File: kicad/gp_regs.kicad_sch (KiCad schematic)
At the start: 12 parts, among them SW2 SW_SPST, SW3 SW_SPST, SW4 SW_SPST, SW5 SW_SPST

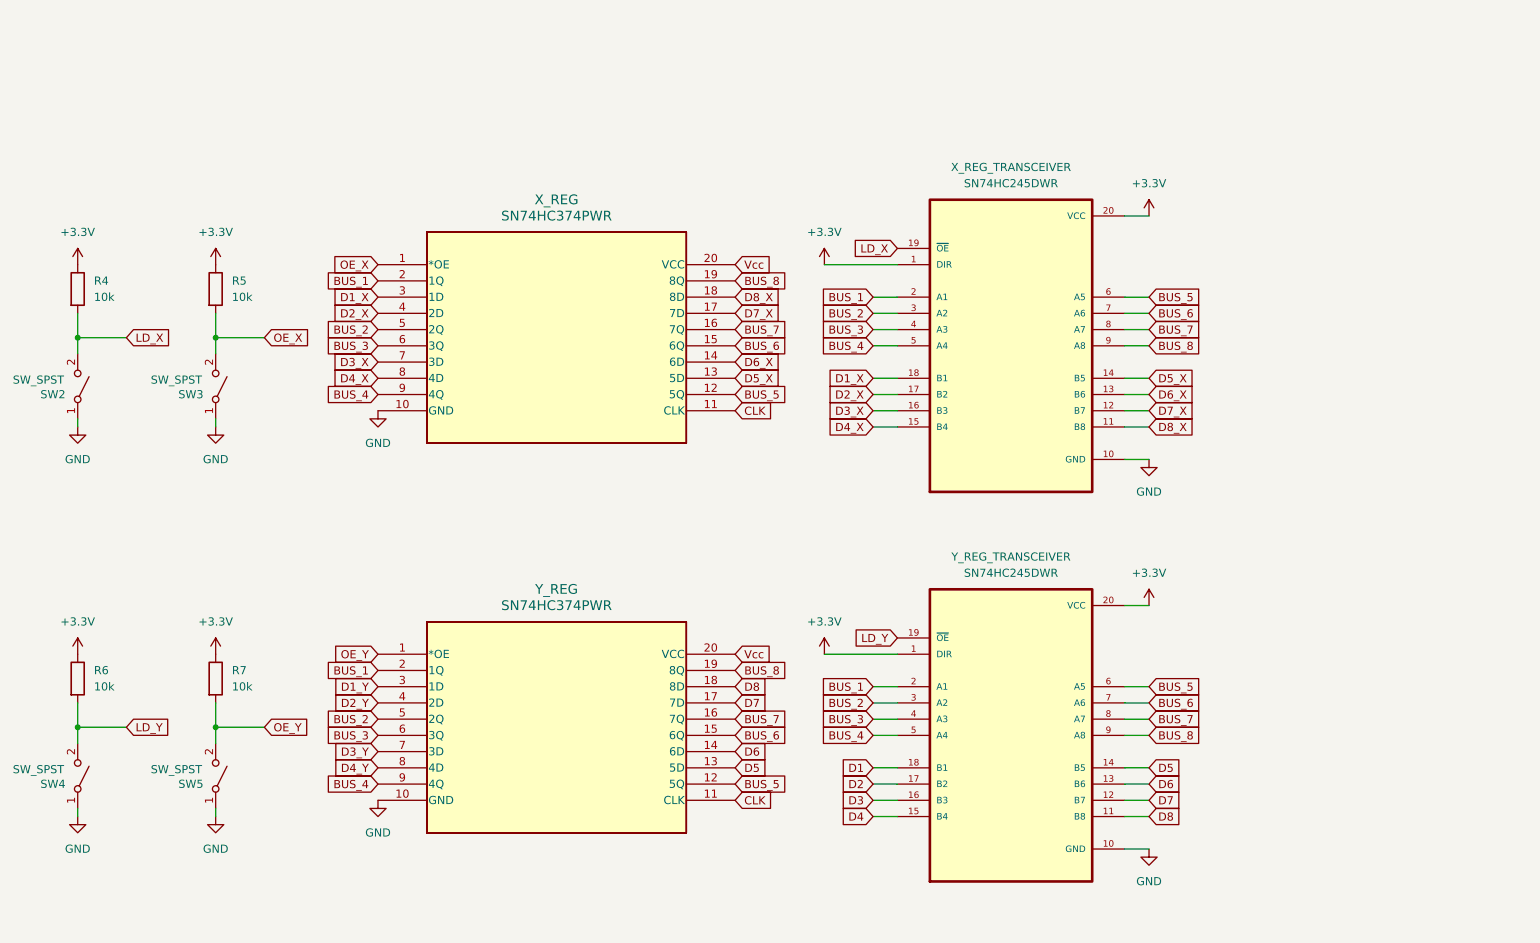
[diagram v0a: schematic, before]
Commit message: update schematic
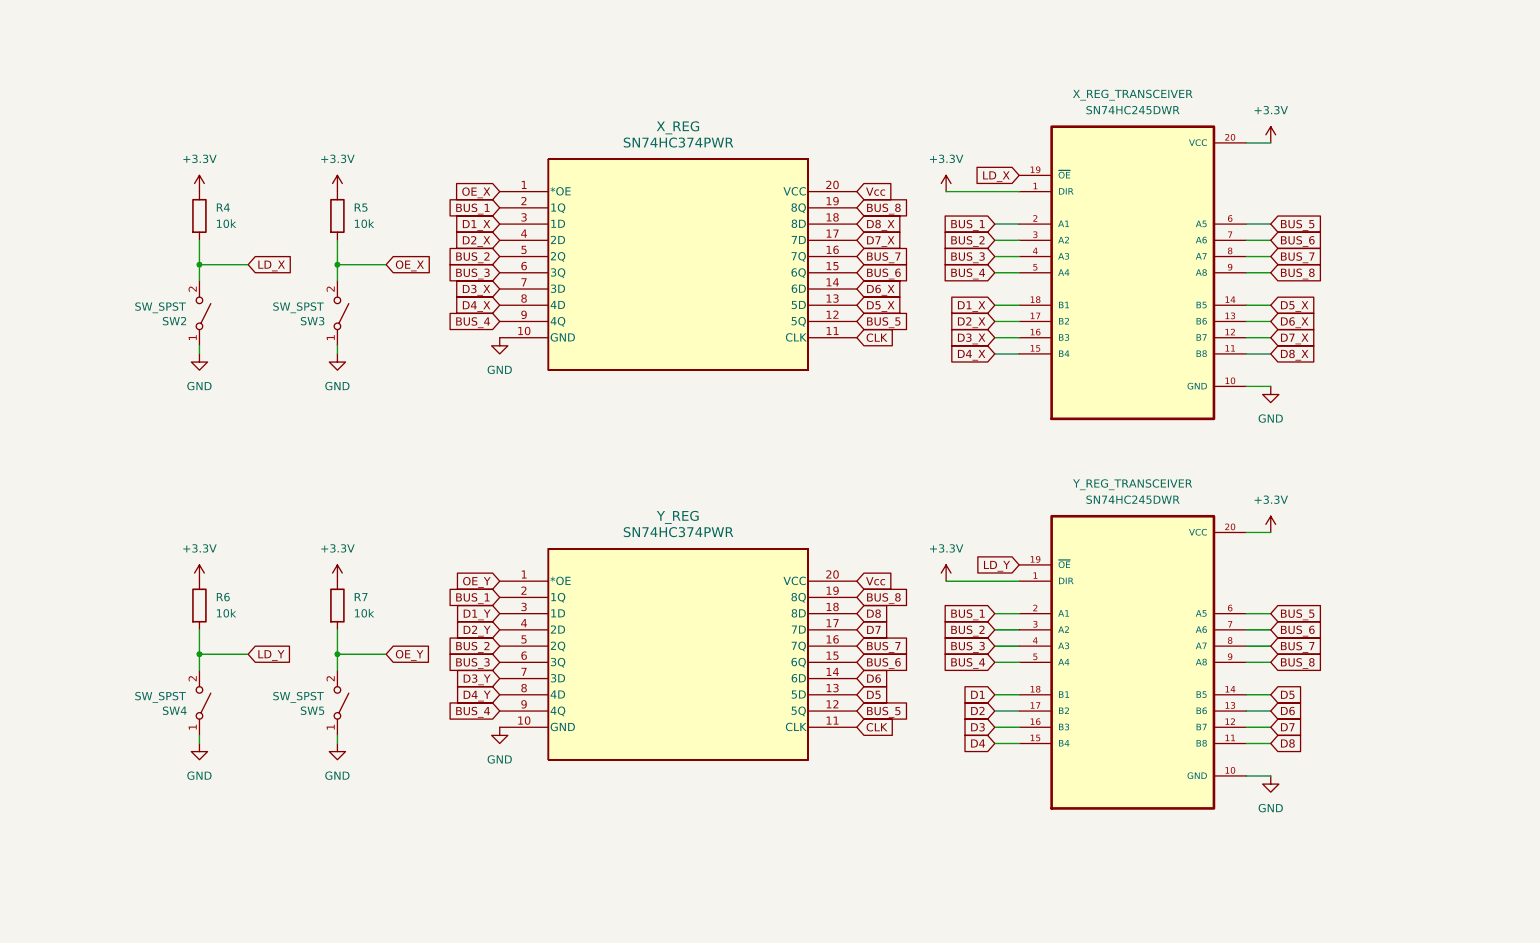
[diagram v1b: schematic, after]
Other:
- moved on the sheet: R4, R5, R6, R7, SW2, SW3, SW4, SW5, X_REG, X_REG_TRANSCEIVER, Y_REG, Y_REG_TRANSCEIVER

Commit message: update schematic
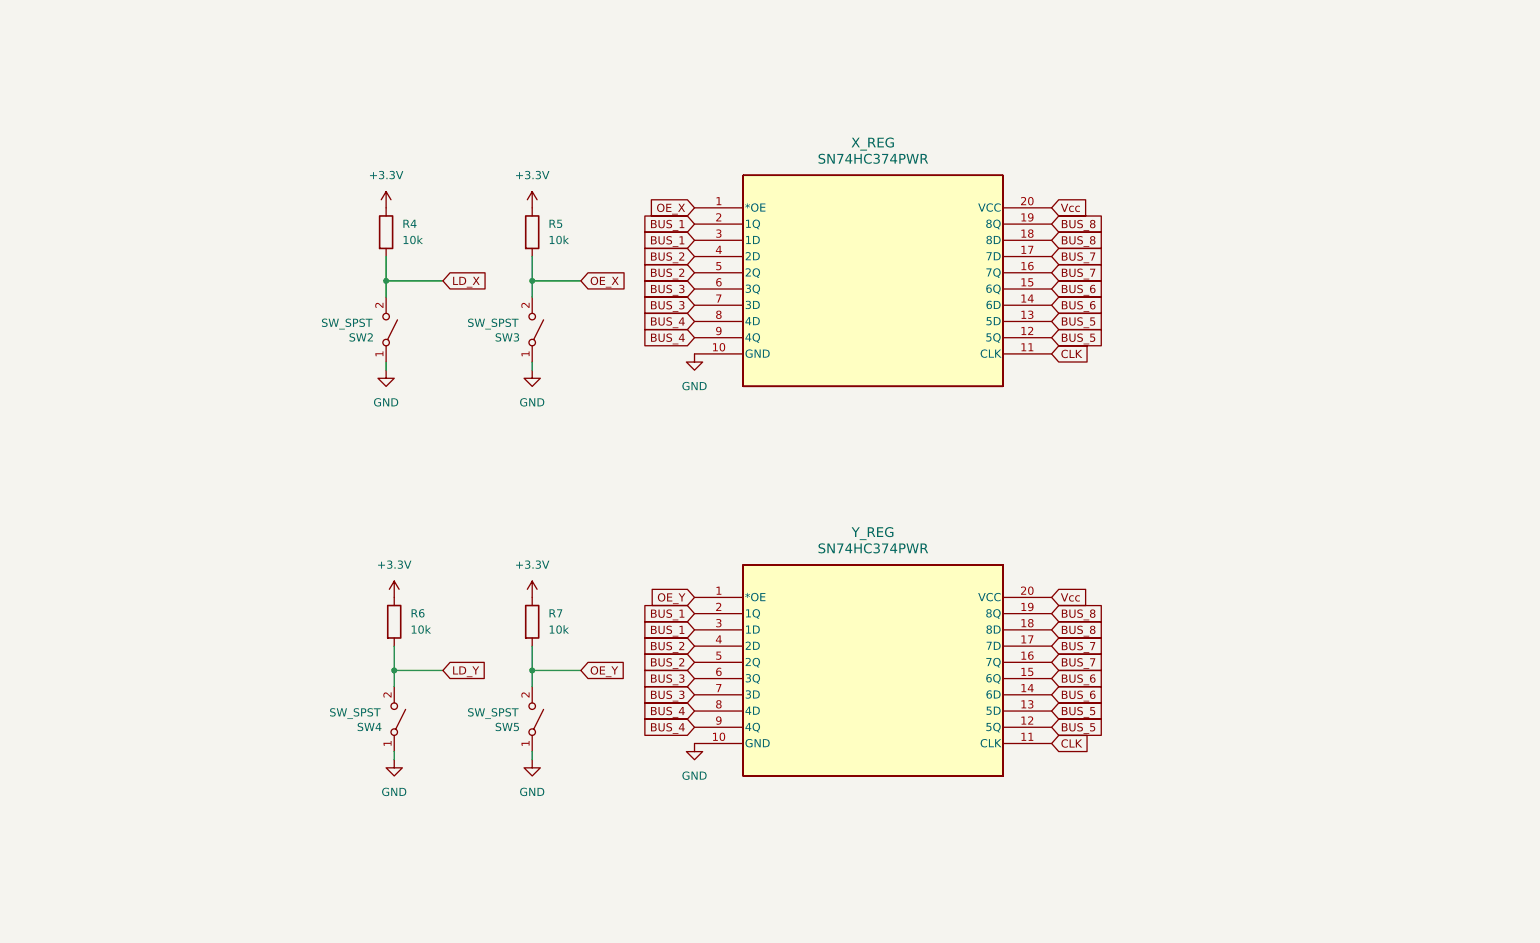
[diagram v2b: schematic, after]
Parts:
- removed X_REG_TRANSCEIVER, Y_REG_TRANSCEIVER: SN74HC245DWR, SN74HC245DWR:SOIC127P1030X265-20N, symbol SN74HC245DWR:SN74HC245DWR
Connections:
- net D1_X is gone; now on net BUS_1: X_REG.3 (1D)
- net D1_Y is gone; now on net BUS_1: Y_REG.3 (1D)
- net D2_X is gone; now on net BUS_2: X_REG.4 (2D)
- net D2_Y is gone; now on net BUS_2: Y_REG.4 (2D)
- net D3_X is gone; now on net BUS_3: X_REG.7 (3D)
- net D3_Y is gone; now on net BUS_3: Y_REG.7 (3D)
- net D4_X is gone; now on net BUS_4: X_REG.8 (4D)
- net D4_Y is gone; now on net BUS_4: Y_REG.8 (4D)
- net D5 is gone; now on net BUS_5: Y_REG.13 (5D)
- net D5_X is gone; now on net BUS_5: X_REG.13 (5D)
- net D6 is gone; now on net BUS_6: Y_REG.14 (6D)
- net D6_X is gone; now on net BUS_6: X_REG.14 (6D)
- net D7 is gone; now on net BUS_7: Y_REG.17 (7D)
- net D7_X is gone; now on net BUS_7: X_REG.17 (7D)
- net D8 is gone; now on net BUS_8: Y_REG.18 (8D)
- net D8_X is gone; now on net BUS_8: X_REG.18 (8D)
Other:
- moved on the sheet: R4, R5, R6, R7, SW2, SW3, SW4, SW5, X_REG, Y_REG

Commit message: update schematic
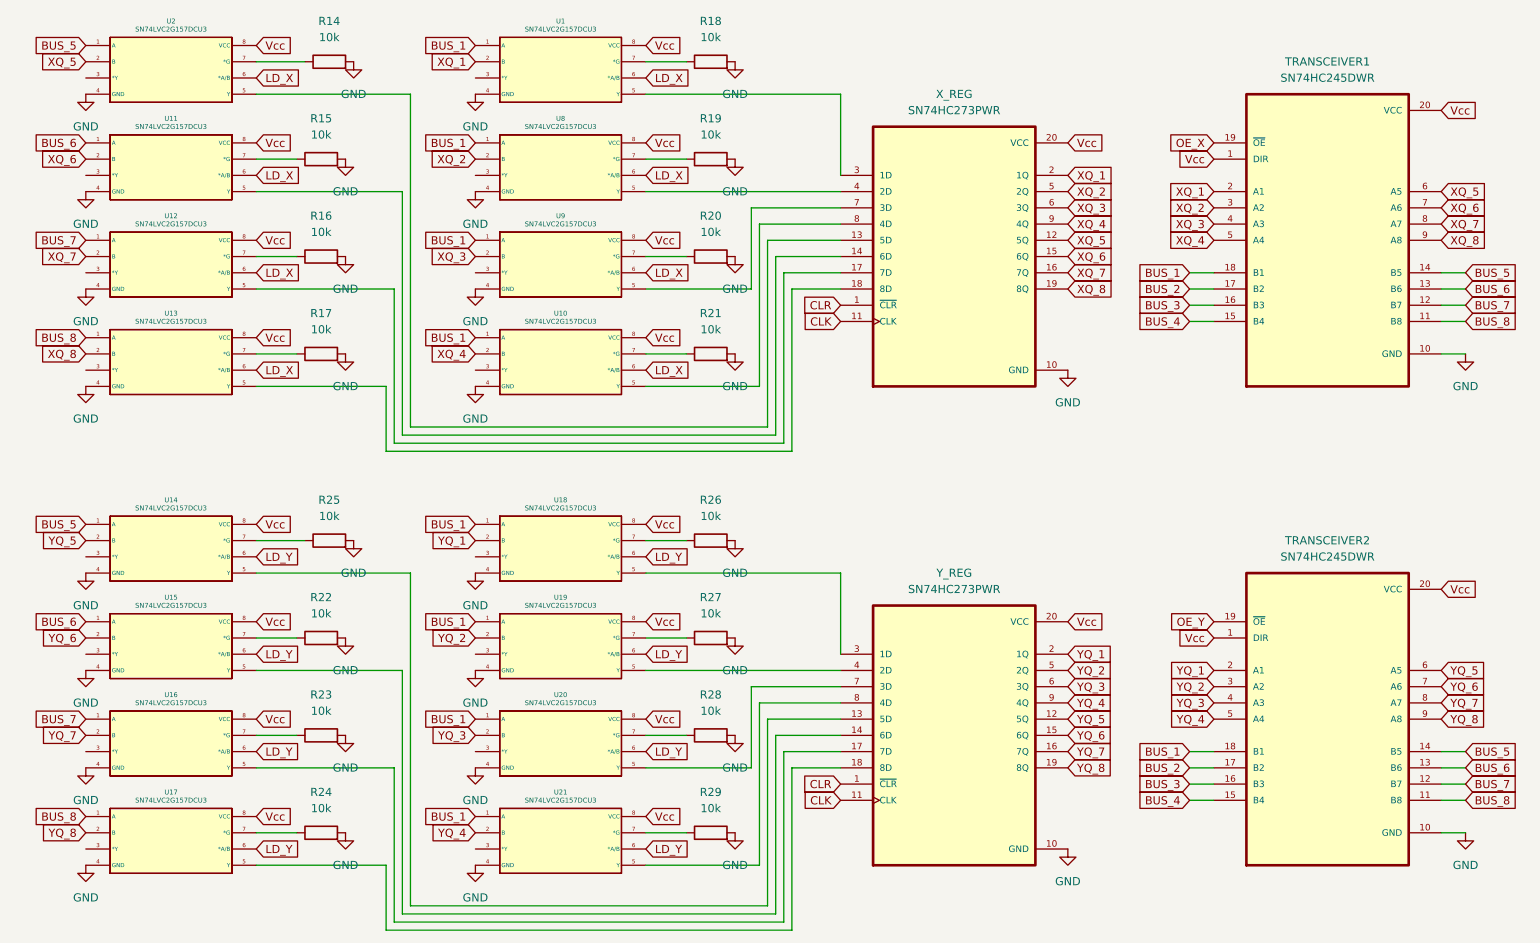
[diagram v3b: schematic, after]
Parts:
- removed R4, R5, R6, R7: 10k, symbol Device:R
- removed SW2, SW3, SW4, SW5: SW_SPST, symbol Switch:SW_SPST
- removed X_REG, Y_REG: SN74HC374PWR, PW20, symbol 2025-07-31_00-00-48:SN74HC374PWR
- added R14, R15, R16, R17, R18, R19, R20, R21, R22, R23, R24, R25, R26, R27, R28, R29: 10k, symbol Device:R
- added TRANSCEIVER1, TRANSCEIVER2: SN74HC245DWR, SN74HC245DWR:SOIC127P1030X265-20N, symbol SN74HC245DWR:SN74HC245DWR
- added U1, U10, U11, U12, U13, U14, U15, U16, U17, U18, U19, U2, U20, U21, U8, U9: SN74LVC2G157DCU3, DCU8, symbol SN74LVC2G157DCU3:SN74LVC2G157DCU3
- added X_REG, Y_REG: SN74HC273PWR, SN74HC273PWR:SOP65P640X120-20N, symbol SN74HC273PWR:SN74HC273PWR
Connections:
- net BUS_1: now also TRANSCEIVER1.18 (B1), TRANSCEIVER2.18 (B1), U1.1 (A), U10.1 (A), U18.1 (A), U19.1 (A), U20.1 (A), U21.1 (A), U8.1 (A), U9.1 (A)
- net BUS_2: now also TRANSCEIVER1.17 (B2), TRANSCEIVER2.17 (B2)
- net BUS_3: now also TRANSCEIVER1.16 (B3), TRANSCEIVER2.16 (B3)
- net BUS_4: now also TRANSCEIVER1.15 (B4), TRANSCEIVER2.15 (B4)
- net BUS_5: now also TRANSCEIVER1.14 (B5), TRANSCEIVER2.14 (B5), U14.1 (A), U2.1 (A)
- net BUS_6: now also TRANSCEIVER1.13 (B6), TRANSCEIVER2.13 (B6), U11.1 (A), U15.1 (A)
- net BUS_7: now also TRANSCEIVER1.12 (B7), TRANSCEIVER2.12 (B7), U12.1 (A), U16.1 (A)
- net BUS_8: now also TRANSCEIVER1.11 (B8), TRANSCEIVER2.11 (B8), U13.1 (A), U17.1 (A)
- net CLK: now also X_REG.11 (CLK), Y_REG.11 (CLK)
- net GND: now also R14.2, R15.2, R16.2, R17.2, R18.2, R19.2, R20.2, R21.2, R22.2, R23.2, R24.2, R25.2, R26.2, R27.2, R28.2, R29.2, TRANSCEIVER1.10 (GND), TRANSCEIVER2.10 (GND), U1.4 (GND), U10.4 (GND), U11.4 (GND), U12.4 (GND), U13.4 (GND), U14.4 (GND), U15.4 (GND), U16.4 (GND), U17.4 (GND), U18.4 (GND), U19.4 (GND), U2.4 (GND), U20.4 (GND), U21.4 (GND), U8.4 (GND), U9.4 (GND), X_REG.10 (GND), Y_REG.10 (GND)
- net LD_X: now also U1.6 (*A/B), U10.6 (*A/B), U11.6 (*A/B), U12.6 (*A/B), U13.6 (*A/B), U2.6 (*A/B), U8.6 (*A/B), U9.6 (*A/B)
- net LD_Y: now also U14.6 (*A/B), U15.6 (*A/B), U16.6 (*A/B), U17.6 (*A/B), U18.6 (*A/B), U19.6 (*A/B), U20.6 (*A/B), U21.6 (*A/B)
- net OE_X: now also TRANSCEIVER1.19 (~{OE})
- net OE_Y: now also TRANSCEIVER2.19 (~{OE})
- net Vcc: now also TRANSCEIVER1.1 (DIR), TRANSCEIVER1.20 (VCC), TRANSCEIVER2.1 (DIR), TRANSCEIVER2.20 (VCC), U1.8 (VCC), U10.8 (VCC), U11.8 (VCC), U12.8 (VCC), U13.8 (VCC), U14.8 (VCC), U15.8 (VCC), U16.8 (VCC), U17.8 (VCC), U18.8 (VCC), U19.8 (VCC), U2.8 (VCC), U20.8 (VCC), U21.8 (VCC), U8.8 (VCC), U9.8 (VCC), X_REG.20 (VCC), Y_REG.20 (VCC)
- new net: R20.1, U9.7 (*G)
- new net: R15.1, U11.7 (*G)
- new net: R24.1, U17.7 (*G)
- new net: U19.5 (Y), Y_REG.4 (2D)
- new net: R27.1, U19.7 (*G)
- new net: R29.1, U21.7 (*G)
- new net: R19.1, U8.7 (*G)
- new net: U15.5 (Y), Y_REG.14 (6D)
- new net: R22.1, U15.7 (*G)
- new net: U10.5 (Y), X_REG.8 (4D)
- new net: R21.1, U10.7 (*G)
- new net: U2.5 (Y), X_REG.13 (5D)
- new net: U11.5 (Y), X_REG.14 (6D)
- new net: U12.5 (Y), X_REG.17 (7D)
- new net: U13.5 (Y), X_REG.18 (8D)
- new net: U1.5 (Y), X_REG.3 (1D)
- new net: U8.5 (Y), X_REG.4 (2D)
- new net: U9.5 (Y), X_REG.7 (3D)
- new net: R23.1, U16.7 (*G)
- new net: U18.5 (Y), Y_REG.3 (1D)
- new net: R26.1, U18.7 (*G)
- new net: U21.5 (Y), Y_REG.8 (4D)
- new net: U17.5 (Y), Y_REG.18 (8D)
- new net: U20.5 (Y), Y_REG.7 (3D)
- new net: R28.1, U20.7 (*G)
- new net: R14.1, U2.7 (*G)
- new net: R16.1, U12.7 (*G)
- new net: R17.1, U13.7 (*G)
- new net: R18.1, U1.7 (*G)
- new net: U16.5 (Y), Y_REG.17 (7D)
- new net: R25.1, U14.7 (*G)
- new net: U14.5 (Y), Y_REG.13 (5D)
- new net CLR: X_REG.1 (~{CLR}), Y_REG.1 (~{CLR})
- new net XQ_1: TRANSCEIVER1.2 (A1), U1.2 (B), X_REG.2 (1Q)
- new net XQ_2: TRANSCEIVER1.3 (A2), U8.2 (B), X_REG.5 (2Q)
- new net XQ_3: TRANSCEIVER1.4 (A3), U9.2 (B), X_REG.6 (3Q)
- new net XQ_4: TRANSCEIVER1.5 (A4), U10.2 (B), X_REG.9 (4Q)
- new net XQ_5: TRANSCEIVER1.6 (A5), U2.2 (B), X_REG.12 (5Q)
- new net XQ_6: TRANSCEIVER1.7 (A6), U11.2 (B), X_REG.15 (6Q)
- new net XQ_7: TRANSCEIVER1.8 (A7), U12.2 (B), X_REG.16 (7Q)
- new net XQ_8: TRANSCEIVER1.9 (A8), U13.2 (B), X_REG.19 (8Q)
- new net YQ_1: TRANSCEIVER2.2 (A1), U18.2 (B), Y_REG.2 (1Q)
- new net YQ_2: TRANSCEIVER2.3 (A2), U19.2 (B), Y_REG.5 (2Q)
- new net YQ_3: TRANSCEIVER2.4 (A3), U20.2 (B), Y_REG.6 (3Q)
- new net YQ_4: TRANSCEIVER2.5 (A4), U21.2 (B), Y_REG.9 (4Q)
- new net YQ_5: TRANSCEIVER2.6 (A5), U14.2 (B), Y_REG.12 (5Q)
- new net YQ_6: TRANSCEIVER2.7 (A6), U15.2 (B), Y_REG.15 (6Q)
- new net YQ_7: TRANSCEIVER2.8 (A7), U16.2 (B), Y_REG.16 (7Q)
- new net YQ_8: TRANSCEIVER2.9 (A8), U17.2 (B), Y_REG.19 (8Q)
